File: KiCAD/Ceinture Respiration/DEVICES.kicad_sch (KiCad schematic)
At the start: 21 parts, among them J4 MEM2061-01-188-00-A_REVA, J5 BUZZER, J9 Oled, M1 Motor_DC, Q1 MMBT3904, SW1 SW_Push, SW2 SW_Push, SW3 SW_Push, SW4 SW_Push, U1 DRV2605LDGS

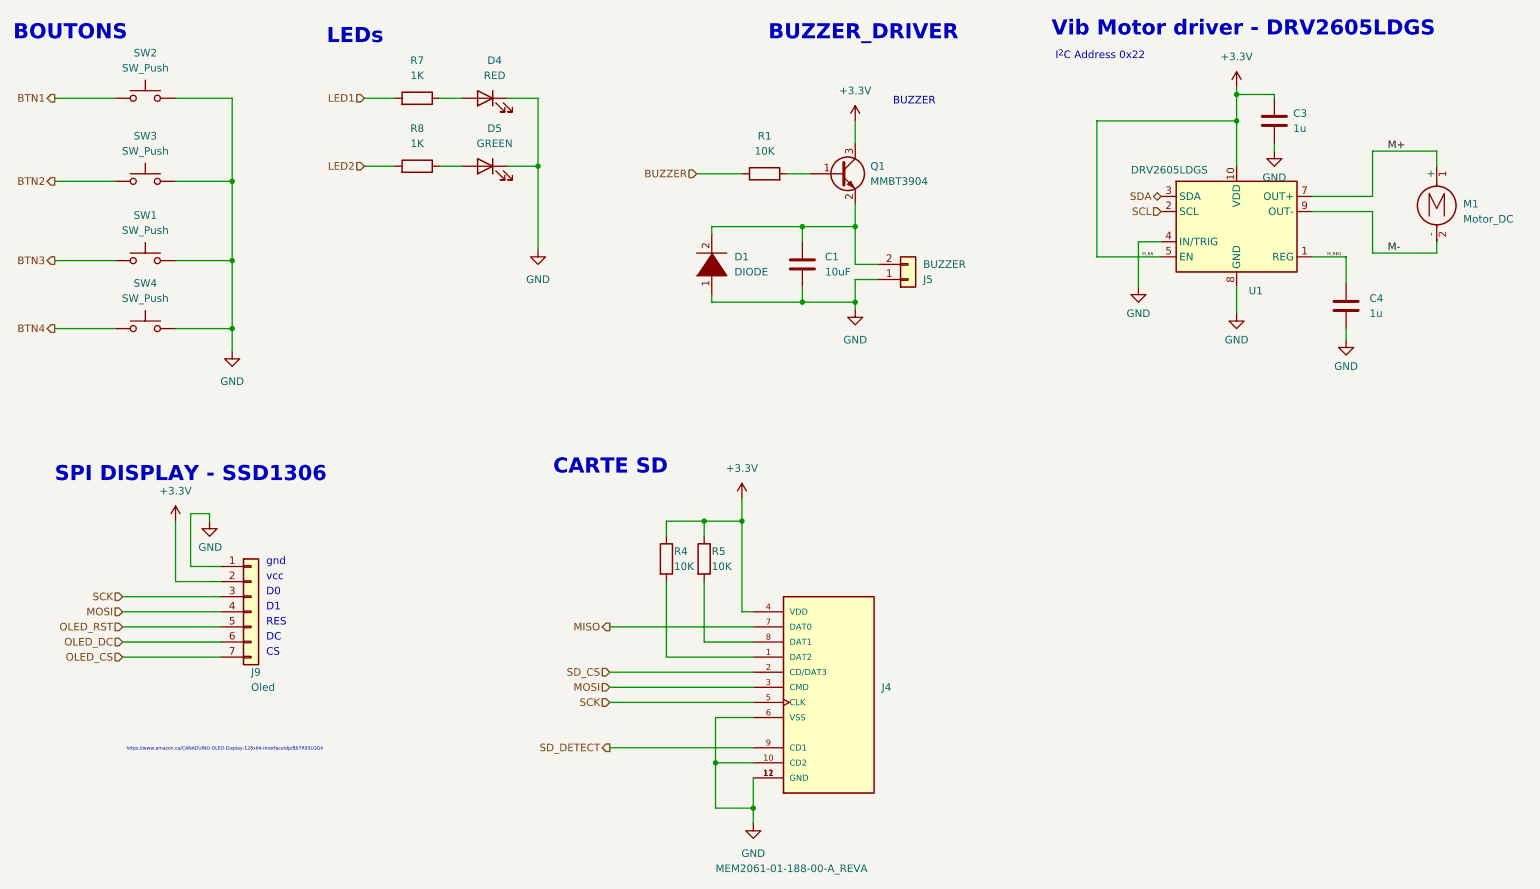
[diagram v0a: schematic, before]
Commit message: Schematique 99%, PCB 50%
schématique complété, nettoyé et layout complété, reste routage
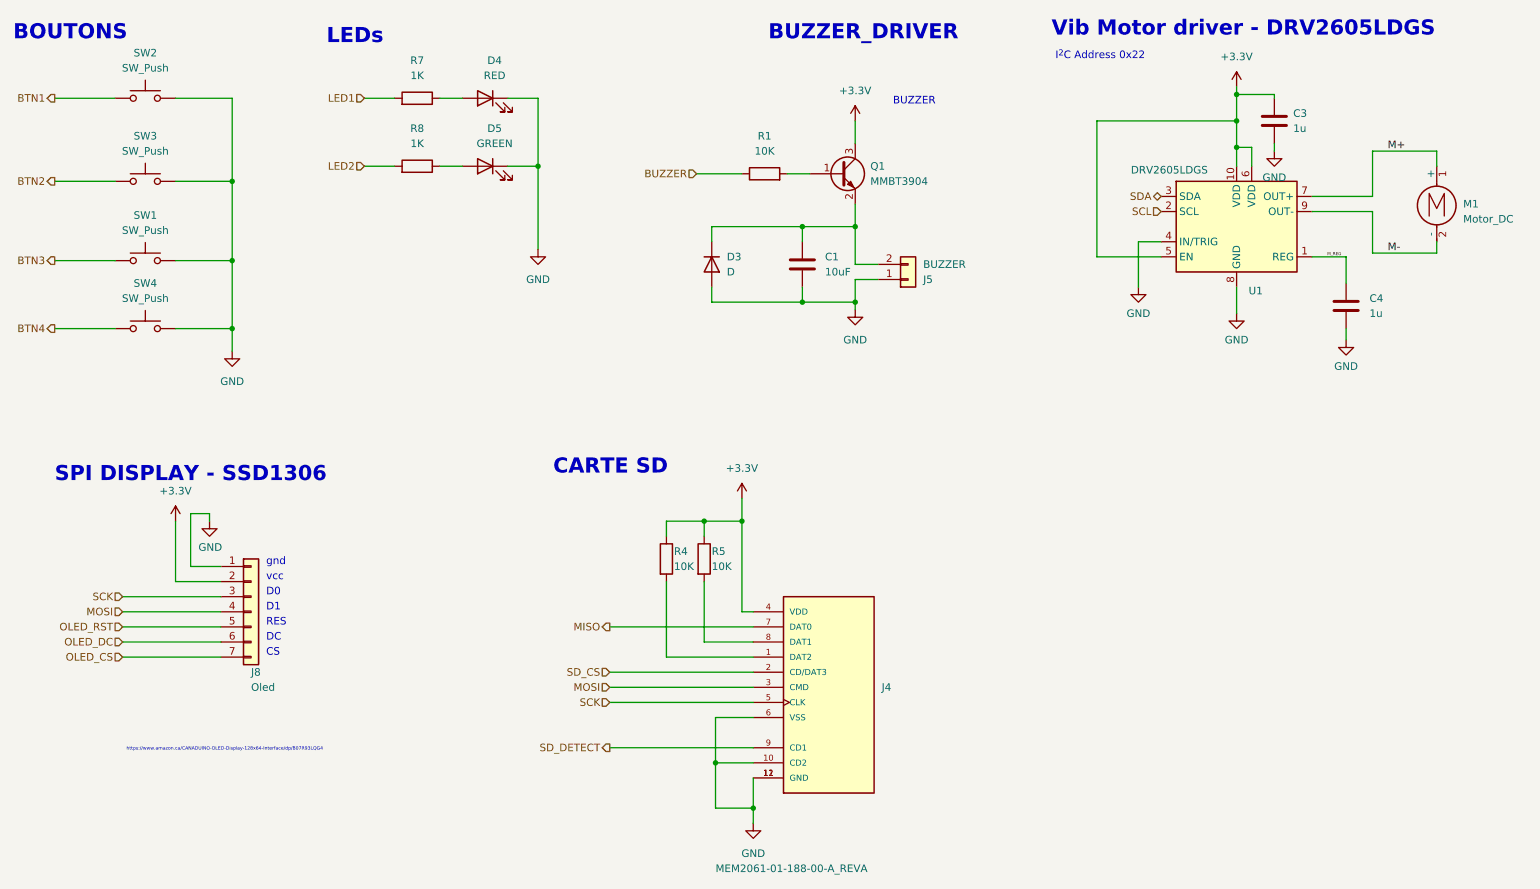
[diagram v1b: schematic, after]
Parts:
- removed D1: DIODE, Diode_SMD:D_SOD-123, symbol pspice:DIODE
- added D3: D, Diode_SMD:D_SOD-323F, symbol Device:D
- J5: footprint Buzzer_Beeper:Buzzer_Murata_PKMCS0909E -> CentureResp:Buzzer_Murata_PKMCS0909E
- M1: footprint Ergowatch:Motor_pad -> CentureResp:XDCR_C0720B001F
- U1: symbol Ergowatch:DRV2605 -> CeintureRespAT:DRV2605
- renumbered J9 to J8
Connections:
- net +3.3V: now also U1.6 (VDD)
- net GND: now also D3.2 (A)
- net at C1.1, J5.2 (Pin_2), Q1.2 (E): now also D3.1 (K)
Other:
- company: (none) -> IngRéadapt UL
- title: (none) -> Modules I/O

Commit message: PCB sent for production
See latest production files.
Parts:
- C1: LCSC (none) -> C96446
- C3, C4: footprint Capacitor_SMD:C_0402_1005Metric -> Capacitor_SMD:C_0603_1608Metric; LCSC C52923 -> C15849
- D3: LCSC (none) -> C191023
- Q1: LCSC (none) -> C20526
- R1, R4, R5: LCSC (none) -> C25804
- R7, R8: LCSC (none) -> C21190
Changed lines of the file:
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@@
+      (effects (font (size 1.27 1.27)) hide)
+    )
+    (property "LCSC" "C25804" (at 134.62 115.57 0)
       (effects (font (size 1.27 1.27)) hide)
     )
@@
       (effects (font (size 1.27 1.27)) hide)
     )
+    (property "LCSC" "C21190" (at 86.36 49.53 0)
+      (effects (font (size 1.27 1.27)) hide)
+    )
     (pin "1")
     (pin "2")
@@
       (effects (font (size 1.27 1.27)) hide)
     )
+    (property "LCSC" "C25804" (at 144.78 50.8 0)
+      (effects (font (size 1.27 1.27)) hide)
+    )
     (pin "1")
     (pin "2")
@@
     )
     (property "Datasheet" "~" (at 86.36 38.1 0)
+      (effects (font (size 1.27 1.27)) hide)
+    )
+    (property "LCSC" "C21190" (at 86.36 38.1 0)
       (effects (font (size 1.27 1.27)) hide)
     )
@@
       (effects (font (size 1.27 1.27)) (justify left))
     )
-    (property "Footprint" "Capacitor_SMD:C_0402_1005Metric" (at 231.4702 45.72 0)
+    (property "Footprint" "Capacitor_SMD:C_0603_1608Metric" (at 231.4702 45.72 0)
       (effects (font (size 1.27 1.27)) hide)
     )
@@
       (effects (font (size 1.27 1.27)) hide)
     )
-    (property "LCSC" "C52923" (at 230.505 41.91 0)
+    (property "LCSC" "C15849" (at 230.505 41.91 0)
       (effects (font (size 1.27 1.27)) hide)
     )
@@
       (effects (font (size 1.27 1.27)) hide)
     )
+    (property "LCSC" "C191023" (at 135.89 66.04 0)
+      (effects (font (size 1.27 1.27)) hide)
+    )
     (pin "1")
     (pin "2")
@@
       (effects (font (size 1.27 1.27)) hide)
     )
+    (property "LCSC" "C25804" (at 128.27 115.57 0)
+      (effects (font (size 1.27 1.27)) hide)
+    )
     (pin "1")
     (pin "2")
@@
       (effects (font (size 1.27 1.27)) (justify left))
     )
-    (property "Footprint" "Capacitor_SMD:C_0402_1005Metric" (at 243.5352 76.835 0)
+    (property "Footprint" "Capacitor_SMD:C_0603_1608Metric" (at 243.5352 76.835 0)
       (effects (font (size 1.27 1.27)) hide)
     )
@@
       (effects (font (size 1.27 1.27)) hide)
     )
-    (property "LCSC" "C52923" (at 242.57 73.025 0)
+    (property "LCSC" "C15849" (at 242.57 73.025 0)
       (effects (font (size 1.27 1.27)) hide)
     )
@@
     )
     (property "Datasheet" "~" (at 151.13 66.04 0)
+      (effects (font (size 1.27 1.27)) hide)
+    )
+    (property "LCSC" "C96446" (at 151.13 66.04 0)
       (effects (font (size 1.27 1.27)) hide)
     )
@@
       (effects (font (size 1.27 1.27)) (justify left) hide)
     )
-    (pin "1")
+    (property "LCSC" "C20526" (at 157.48 50.8 0)
+      (effects (font (size 1.27 1.27)) hide)
+    )
+    (pin "1")
